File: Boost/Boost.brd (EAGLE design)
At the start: 100 x 80 mm, 2 parts

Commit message: boost
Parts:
- added C1: 10nF, adafruit:E2,5-5
- added C2, C4, C5, C6: 22uF, adafruit:E2,5-5
- added JP1: (no value), adafruit:1X03
- added JP2: M02PTH, SparkFun-Connectors:1X02
- added L1: 1uH, eagle-ltspice:0207/10
- added R3: 1M Ohm, adafruit:0207/10
- moved TPS61230 47.2 mm to (7.62, 20.3)
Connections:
- new net N$1: C1.-, C4.-, C6.-, JP1.1, JP2.2, TPS61230.11
- new net N$10: C2.-, C5.+
- new net N$2: R3.1, TPS61230.5
- new net N$3: L1.2, TPS61230.1, TPS61230.2
- new net N$4: C2.+, JP1.3, R3.2, TPS61230.3, TPS61230.4
- new net N$5: JP1.2, TPS61230.7
- new net N$7: C1.+, TPS61230.6
- new net N$8: C4.+, JP2.1, L1.1, TPS61230.10, TPS61230.9
- new net N$9: C5.-, C6.+
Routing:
- net N$1: track 0.00 -> 64.2 mm
- net N$8: track 0.00 -> 31.3 mm
- net N$5: track 0.00 -> 28.8 mm
- net N$4: track 0.00 -> 27.8 mm, vias 0 -> 1
- net N$3: track 0.00 -> 15.6 mm
- net N$7: track 0.00 -> 13.4 mm, vias 0 -> 1
- net N$9: track 0.00 -> 8.49 mm
- net N$2: track 0.00 -> 8.29 mm
- net N$10: track 0.00 -> 5.08 mm
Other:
- board size 100 x 80 mm -> 14.9 x 38.1 mm

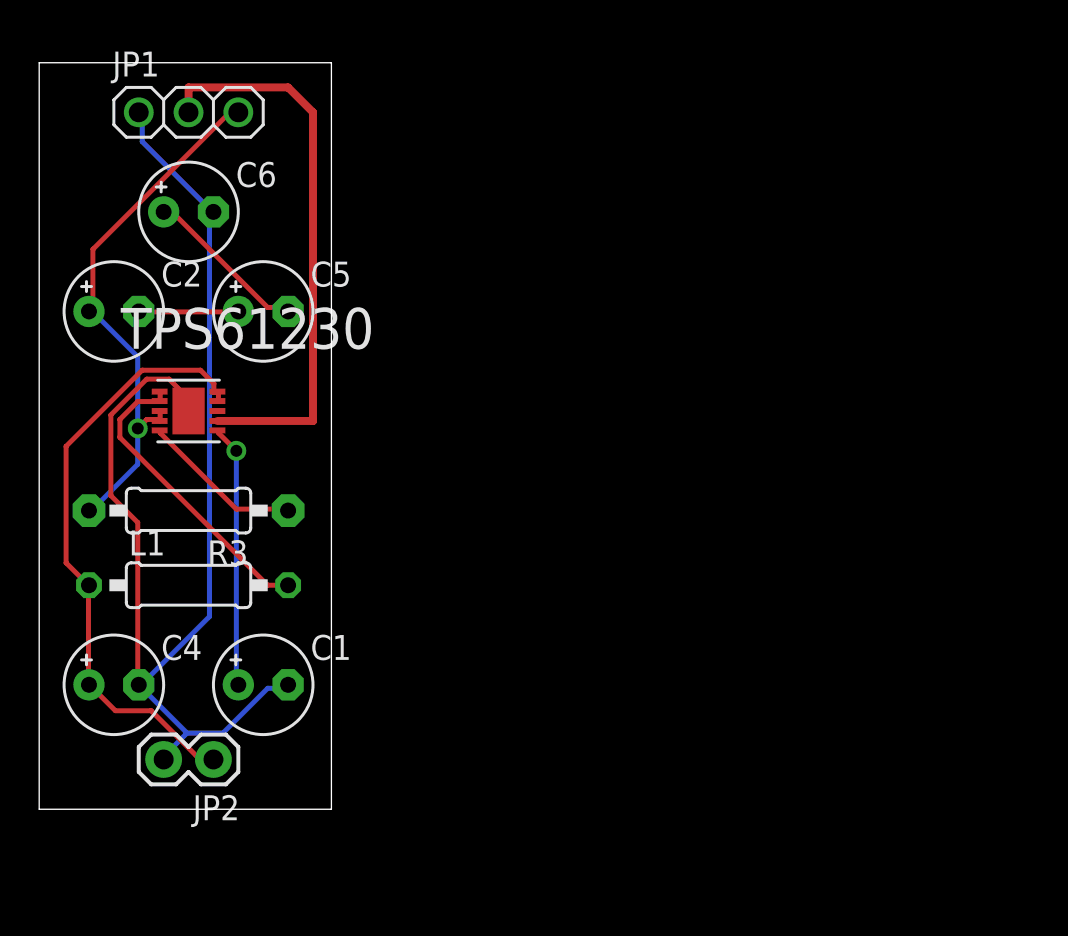
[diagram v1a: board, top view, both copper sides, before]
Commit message: Made some changes to feedback loop and reorganized controller
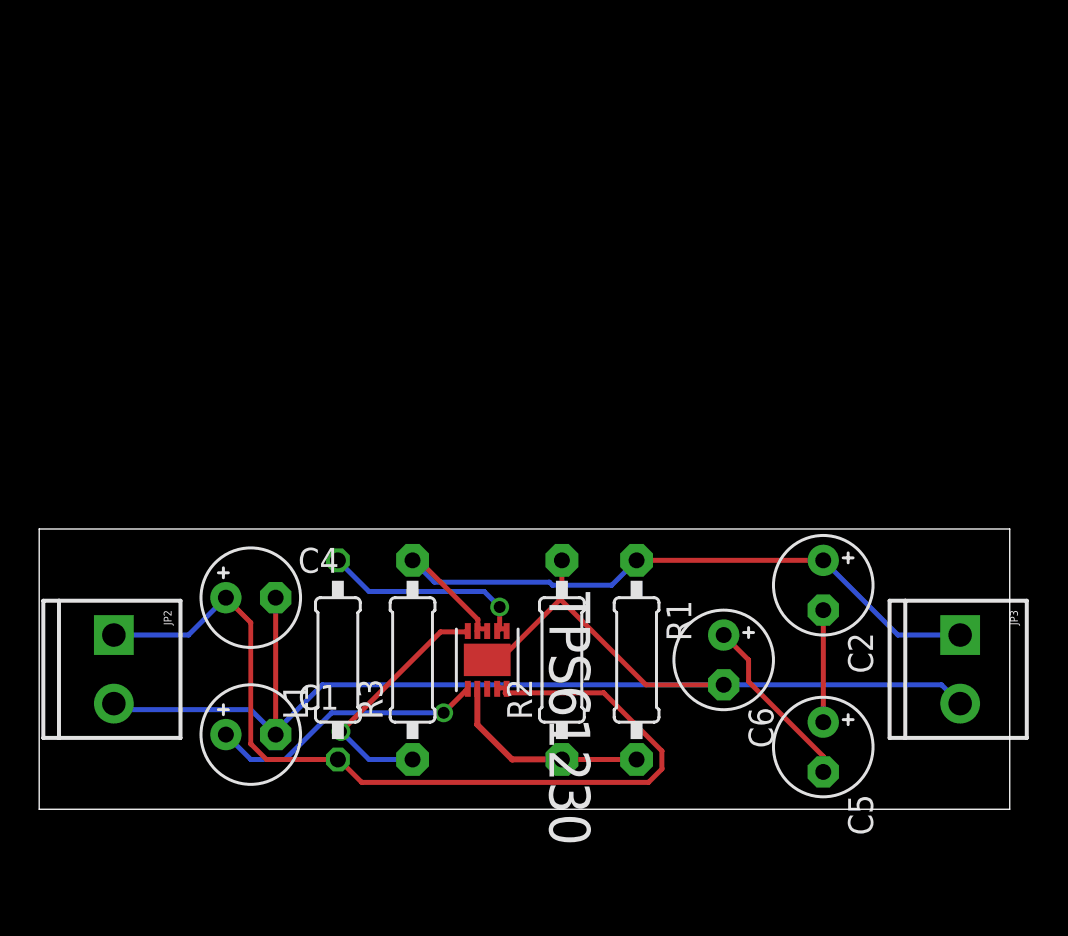
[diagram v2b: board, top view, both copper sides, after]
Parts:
- removed JP1: (no value), adafruit:1X03
- added JP3: M023.5MM, SparkFun-Connectors:SCREWTERMINAL-3.5MM-2
- added R1: 402 kOhm, adafruit:0207/10
- added R2: 100 kOhm, adafruit:0207/10
- JP2: value M02PTH -> M023.5MM; device SparkFun-Connectors:1X02 -> SparkFun-Connectors:SCREWTERMINAL-3.5MM-2
- moved C2 38.8 mm to (40.0, 11.4), turned to 270 degrees
- moved C5 36.2 mm to (40.0, 3.17), turned to 270 degrees
- moved C6 35.6 mm to (34.9, 7.62), turned to 270 degrees
- moved TPS61230 19.8 mm to (22.9, 7.62), turned to 270 degrees
- moved R3 13.7 mm to (19.1, 7.62), turned to 90 degrees
- moved L1 8.52 mm to (15.2, 7.62), turned to 90 degrees
- moved C4 8.28 mm to (10.8, 10.8)
- moved JP2 8.13 mm to (3.81, 8.89), turned to 270 degrees
- moved C1 2.62 mm to (10.8, 3.81)
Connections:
- removed net N$5: JP1.2, TPS61230.7
- new net N$11: R1.2, R2.1, TPS61230.7
- net N$1: now also JP3.2, R2.2; no longer JP1.1
- net N$4: now also JP3.1, R1.1; no longer JP1.3
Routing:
- net N$5: track 28.8 -> 0.00 mm
- net N$8: track 31.3 -> 47.4 mm
- net N$11: track 0.00 -> 10.7 mm
- net N$4: track 27.8 -> 36.3 mm, vias 1 -> 0
- net N$1: track 64.2 -> 69.6 mm
- net N$3: track 15.6 -> 11.0 mm, vias 0 -> 1
- net N$2: track 8.29 -> 12.8 mm, vias 0 -> 1
- net N$7: track 13.4 -> 14.4 mm
- net N$10: track 5.08 -> 5.71 mm
- net N$9: track 8.49 -> 9.09 mm
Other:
- board size 14.9 x 38.1 mm -> 49.5 x 14.3 mm
